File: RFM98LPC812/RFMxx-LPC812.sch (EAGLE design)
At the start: 21 parts, among them X1 BU-SMA-V, X2 BU-SMA-V

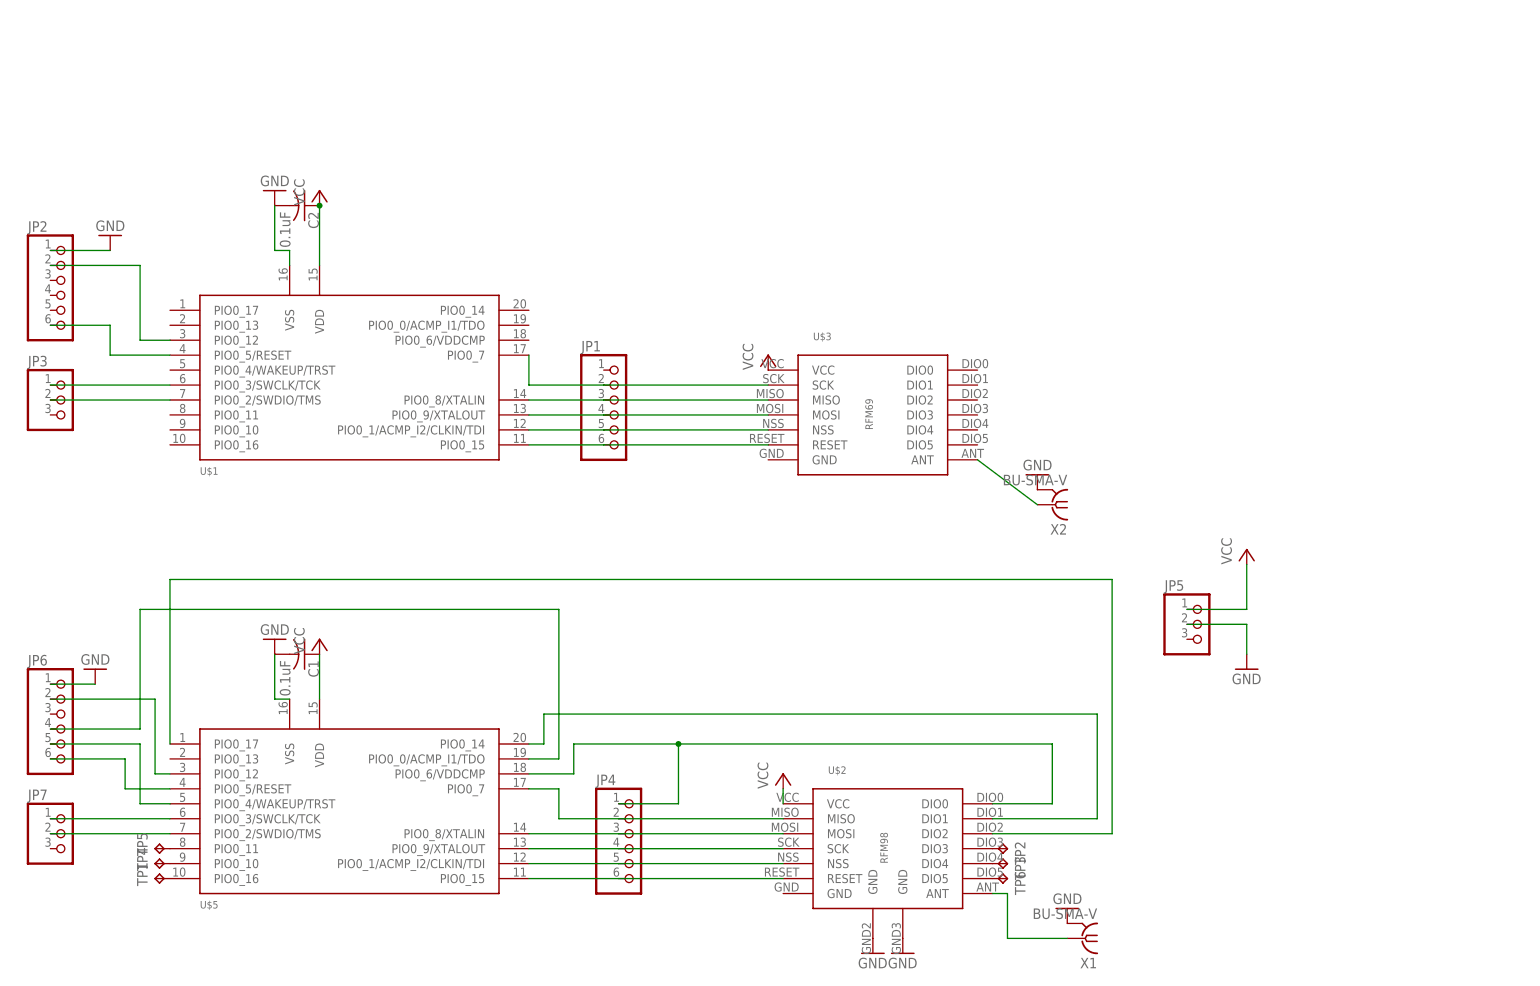
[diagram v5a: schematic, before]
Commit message: LEDs on DIO0
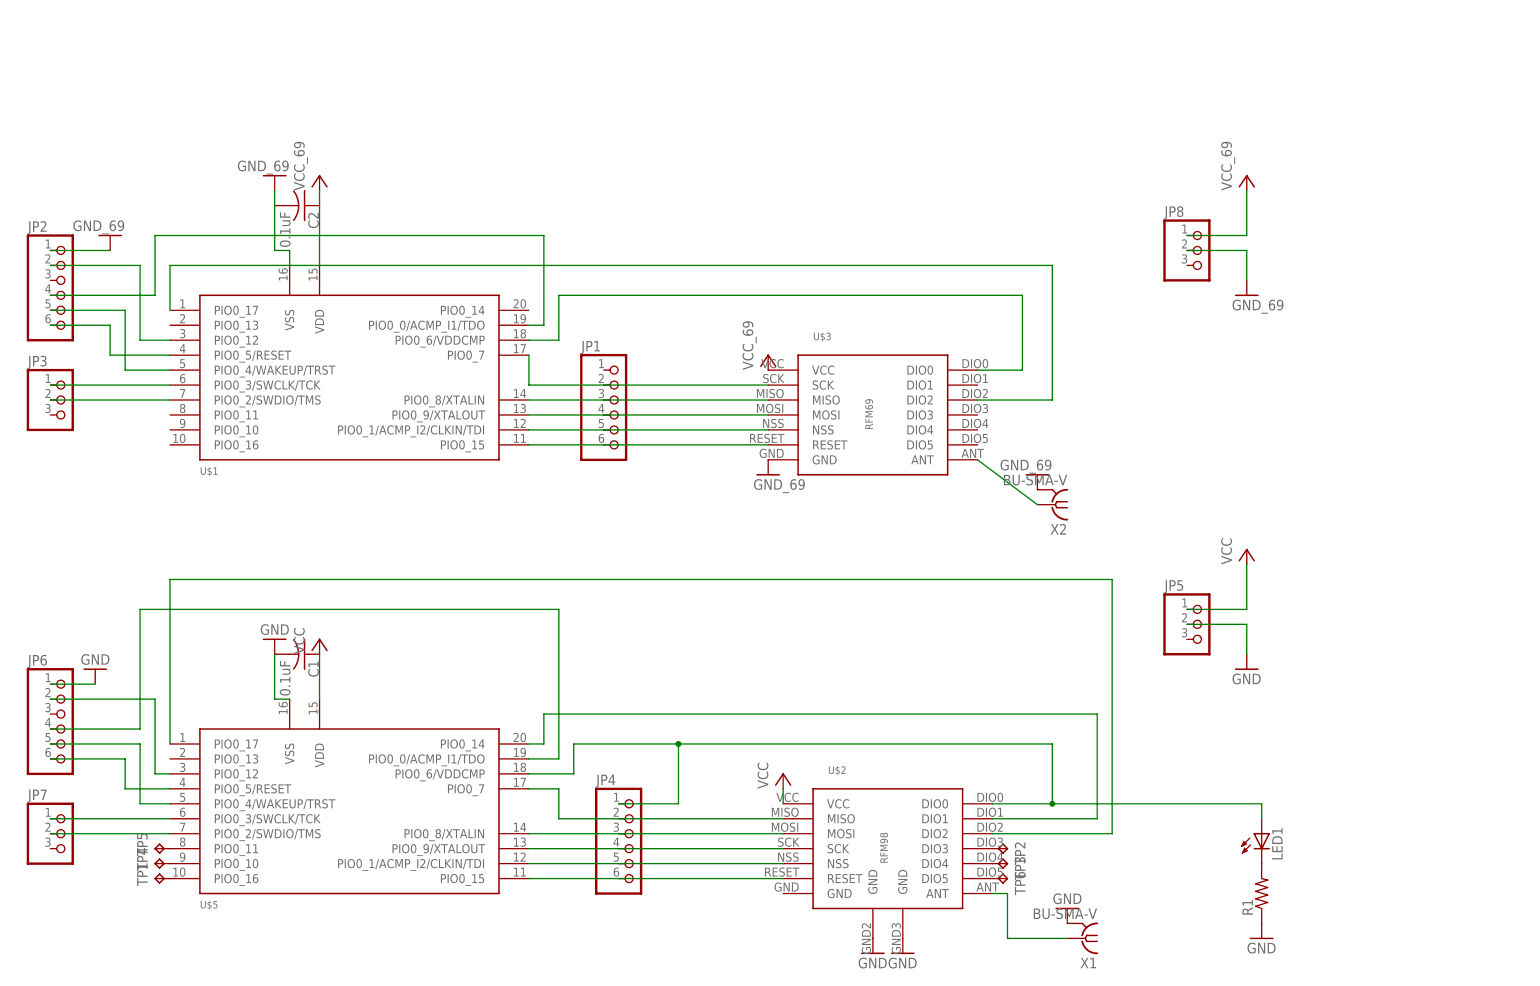
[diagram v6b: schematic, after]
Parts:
- added JP8: (no value), adafruit:PINHD-1X3
- added LED1: (no value), adafruit:LEDCHIP-LED0805
- added R1: (no value), resistor:R-US_R0805
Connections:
- new net N$2: JP2.5, U$1.PIO0_4/WAKEUP/TRST
- new net N$24: U$1.PIO0_6/VDDCMP, U$3.DIO0
- new net N$35: JP2.4, U$1.PIO0_0/ACMP_I1/TDO
- new net N$36: U$1.PIO0_17, U$3.DIO2
- new net N$37: LED1.C, R1.2
- net GND: now also JP8.2, R1.1, U$3.GND
- net N$22: now also LED1.A
- net VCC: now also JP8.1
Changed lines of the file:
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@@
 <part name="TP5" library="testpad" deviceset="TP" device="B1,27"/>
 <part name="TP6" library="testpad" deviceset="TP" device="B1,27"/>
-<part name="GND1" library="supply1" deviceset="GND" device=""/>
+<part name="GND1" library="supply1" deviceset="GND" device="" value="GND_69"/>
 <part name="C2" library="adafruit" deviceset="C-US" device="C0805" value="0.1uF"/>
-<part name="GND2" library="supply1" deviceset="GND" device=""/>
-<part name="P+2" library="supply1" deviceset="VCC" device=""/>
 <part name="JP3" library="adafruit" deviceset="PINHD-1X3" device=""/>
+<part name="GND3" library="supply1" deviceset="GND" device="" value="GND_69"/>
+<part name="GND4" library="supply1" deviceset="GND" device="" value="GND_69"/>
+<part name="JP8" library="adafruit" deviceset="PINHD-1X3" device=""/>
+<part name="GND5" library="supply1" deviceset="GND" device="" value="GND_69"/>
+<part name="P+5" library="supply1" deviceset="VCC" device="" value="VCC_69"/>
+<part name="P+2" library="supply1" deviceset="VCC" device="" value="VCC_69"/>
+<part name="GND2" library="supply1" deviceset="GND" device="" value="GND_69"/>
+<part name="P+6" library="supply1" deviceset="VCC" device="" value="VCC_69"/>
+<part name="LED1" library="adafruit" deviceset="LED" device="CHIP-LED0805"/>
 <part name="GND_RFM4" library="supply1" deviceset="GND" device=""/>
-<part name="P+5" library="supply1" deviceset="VCC" device=""/>
+<part name="R1" library="resistor" deviceset="R-US_" device="R0805"/>
 </parts>
 <sheets>
@@
 <instance part="GND1" gate="1" x="-129.54" y="71.12" rot="R180"/>
 <instance part="C2" gate="G$1" x="-96.52" y="76.2" rot="R270"/>
-<instance part="GND2" gate="1" x="-101.6" y="78.74" rot="R180"/>
-<instance part="P+2" gate="VCC" x="-93.98" y="78.74"/>
 <instance part="JP3" gate="A" x="-137.16" y="43.18"/>
-<instance part="GND_RFM4" gate="1" x="27.94" y="30.48" rot="R180"/>
+<instance part="GND3" gate="1" x="-17.78" y="30.48"/>
+<instance part="GND4" gate="1" x="27.94" y="30.48" rot="R180"/>
+<instance part="JP8" gate="A" x="55.88" y="68.58"/>
+<instance part="GND5" gate="1" x="63.5" y="60.96"/>
 <instance part="P+5" gate="VCC" x="-17.78" y="50.8"/>
+<instance part="P+2" gate="VCC" x="-93.98" y="81.28"/>
+<instance part="GND2" gate="1" x="-101.6" y="81.28" rot="R180"/>
+<instance part="P+6" gate="VCC" x="63.5" y="81.28"/>
+<instance part="LED1" gate="G$1" x="66.04" y="-30.48"/>
+<instance part="GND_RFM4" gate="1" x="66.04" y="-48.26"/>
+<instance part="R1" gate="G$1" x="66.04" y="-40.64" rot="R90"/>
 </instances>
 <busses>
@@
 </segment>
 <segment>
+<pinref part="U$3" gate="G$1" pin="VCC"/>
+<pinref part="P+5" gate="VCC" pin="VCC"/>
+</segment>
+<segment>
 <pinref part="U$1" gate="G$1" pin="VDD"/>
 <pinref part="C2" gate="G$1" pin="1"/>
 <wire x1="-93.98" y1="66.04" x2="-93.98" y2="76.2" width="0.1524" layer="91"/>
+<wire x1="-93.98" y1="78.74" x2="-93.98" y2="76.2" width="0.1524" layer="91"/>
 <pinref part="P+2" gate="VCC" pin="VCC"/>
-<junction x="-93.98" y="76.2"/>
-</segment>
-<segment>
-<pinref part="U$3" gate="G$1" pin="VCC"/>
-<pinref part="P+5" gate="VCC" pin="VCC"/>
+</segment>
+<segment>
+<pinref part="JP8" gate="A" pin="1"/>
+<pinref part="P+6" gate="VCC" pin="VCC"/>
+<wire x1="53.34" y1="71.12" x2="63.5" y2="71.12" width="0.1524" layer="91"/>
+<wire x1="63.5" y1="71.12" x2="63.5" y2="78.74" width="0.1524" layer="91"/>
 </segment>
 </net>
@@
 </segment>
 <segment>
+<pinref part="U$3" gate="G$1" pin="GND"/>
+<pinref part="GND3" gate="1" pin="GND"/>
+</segment>
+<segment>
+<pinref part="X2" gate="G$1" pin="2"/>
+<pinref part="GND4" gate="1" pin="GND"/>
+</segment>
+<segment>
+<pinref part="JP8" gate="A" pin="2"/>
+<pinref part="GND5" gate="1" pin="GND"/>
+<wire x1="53.34" y1="68.58" x2="63.5" y2="68.58" width="0.1524" layer="91"/>
+<wire x1="63.5" y1="68.58" x2="63.5" y2="63.5" width="0.1524" layer="91"/>
+</segment>
+<segment>
 <pinref part="C2" gate="G$1" pin="2"/>
-<pinref part="GND2" gate="1" pin="GND"/>
 <pinref part="U$1" gate="G$1" pin="VSS"/>
 <wire x1="-99.06" y1="66.04" x2="-99.06" y2="68.58" width="0.1524" layer="91"/>
 <wire x1="-99.06" y1="68.58" x2="-101.6" y2="68.58" width="0.1524" layer="91"/>
 <wire x1="-101.6" y1="68.58" x2="-101.6" y2="76.2" width="0.1524" layer="91"/>
-</segment>
-<segment>
-<pinref part="X2" gate="G$1" pin="2"/>
+<wire x1="-101.6" y1="78.74" x2="-101.6" y2="76.2" width="0.1524" layer="91"/>
+<pinref part="GND2" gate="1" pin="GND"/>
+</segment>
+<segment>
 <pinref part="GND_RFM4" gate="1" pin="GND"/>
+<pinref part="R1" gate="G$1" pin="1"/>
 </segment>
 </net>
@@
 <wire x1="-50.8" y1="-20.32" x2="-58.42" y2="-20.32" width="0.1524" layer="91"/>
 <junction x="-33.02" y="-15.24"/>
+<wire x1="30.48" y1="-25.4" x2="66.04" y2="-25.4" width="0.1524" layer="91"/>
+<pinref part="LED1" gate="G$1" pin="A"/>
+<wire x1="66.04" y1="-25.4" x2="66.04" y2="-27.94" width="0.1524" layer="91"/>
+<junction x="30.48" y="-25.4"/>
 </segment>
 </net>
@@
 </segment>
 </net>
+<net name="N$2" class="0">
+<segment>
+<pinref part="JP2" gate="A" pin="5"/>
+<wire x1="-139.7" y1="58.42" x2="-127" y2="58.42" width="0.1524" layer="91"/>
+<wire x1="-127" y1="58.42" x2="-127" y2="48.26" width="0.1524" layer="91"/>
+<pinref part="U$1" gate="G$1" pin="PIO0_4/WAKEUP/TRST"/>
+<wire x1="-127" y1="48.26" x2="-119.38" y2="48.26" width="0.1524" layer="91"/>
+</segment>
+</net>
+<net name="N$24" class="0">
+<segment>
+<pinref part="U$3" gate="G$1" pin="DIO0"/>
+<wire x1="17.78" y1="48.26" x2="25.4" y2="48.26" width="0.1524" layer="91"/>
+<wire x1="25.4" y1="48.26" x2="25.4" y2="60.96" width="0.1524" layer="91"/>
+<wire x1="25.4" y1="60.96" x2="-53.34" y2="60.96" width="0.1524" layer="91"/>
+<wire x1="-53.34" y1="60.96" x2="-53.34" y2="53.34" width="0.1524" layer="91"/>
+<pinref part="U$1" gate="G$1" pin="PIO0_6/VDDCMP"/>
+<wire x1="-53.34" y1="53.34" x2="-58.42" y2="53.34" width="0.1524" layer="91"/>
+</segment>
+</net>
+<net name="N$36" class="0">
+<segment>
+<pinref part="U$3" gate="G$1" pin="DIO2"/>
+<wire x1="17.78" y1="43.18" x2="30.48" y2="43.18" width="0.1524" layer="91"/>
+<wire x1="30.48" y1="43.18" x2="30.48" y2="66.04" width="0.1524" layer="91"/>
+<wire x1="30.48" y1="66.04" x2="-119.38" y2="66.04" width="0.1524" layer="91"/>
+<pinref part="U$1" gate="G$1" pin="PIO0_17"/>
+<wire x1="-119.38" y1="66.04" x2="-119.38" y2="58.42" width="0.1524" layer="91"/>
+</segment>
+</net>
+<net name="N$35" class="0">
+<segment>
+<pinref part="JP2" gate="A" pin="4"/>
+<wire x1="-139.7" y1="60.96" x2="-121.92" y2="60.96" width="0.1524" layer="91"/>
+<wire x1="-121.92" y1="60.96" x2="-121.92" y2="71.12" width="0.1524" layer="91"/>
+<wire x1="-121.92" y1="71.12" x2="-55.88" y2="71.12" width="0.1524" layer="91"/>
+<wire x1="-55.88" y1="71.12" x2="-55.88" y2="55.88" width="0.1524" layer="91"/>
+<pinref part="U$1" gate="G$1" pin="PIO0_0/ACMP_I1/TDO"/>
+<wire x1="-55.88" y1="55.88" x2="-58.42" y2="55.88" width="0.1524" layer="91"/>
+</segment>
+</net>
+<net name="N$37" class="0">
+<segment>
+<pinref part="R1" gate="G$1" pin="2"/>
+<pinref part="LED1" gate="G$1" pin="C"/>
+</segment>
+</net>
